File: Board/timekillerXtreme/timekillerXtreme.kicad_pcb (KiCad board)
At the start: 2 copper layers, 61.5 x 105.2 mm, 98 parts, among them J1 Battery, J10 Conn_01x02, J11 TP_USB, J12 PROG, J13 CONN_01X03, J14 TP_3.3V, J15 PE7, J16 PE8, J17 PE9, J18 PE10, J19 PD4, J2 USB_OTG, J20 PD1, J21 PD0, J22 PD3, J23 PE11, J24 Pb12, J3 Conn_Bottom_Expansion, J4 Conn_Internal_Expansion, J5 Conn_LCD_Board, J6 uSD, J7 CAPTEST, J8 TP_AUDIO_R, J9 TP_AUDIO_L, Q1 IRLML6302, Q2 PMBT3904.215, SW1 PWR, SW2 A, SW3 B, SW4 LEFT, SW5 RIGHT, SW6 DOWN, SW7 UP, SW8 RST, U1 MCP73831, U2 FT230XS-R, U3 NCP1529, U5 STM32F407VGT6, U6 USBLC6, U7 AOZ1310, U8 USBLC6, U9 USBLC6, Y1 32.768 KHz, Y2 16MHz

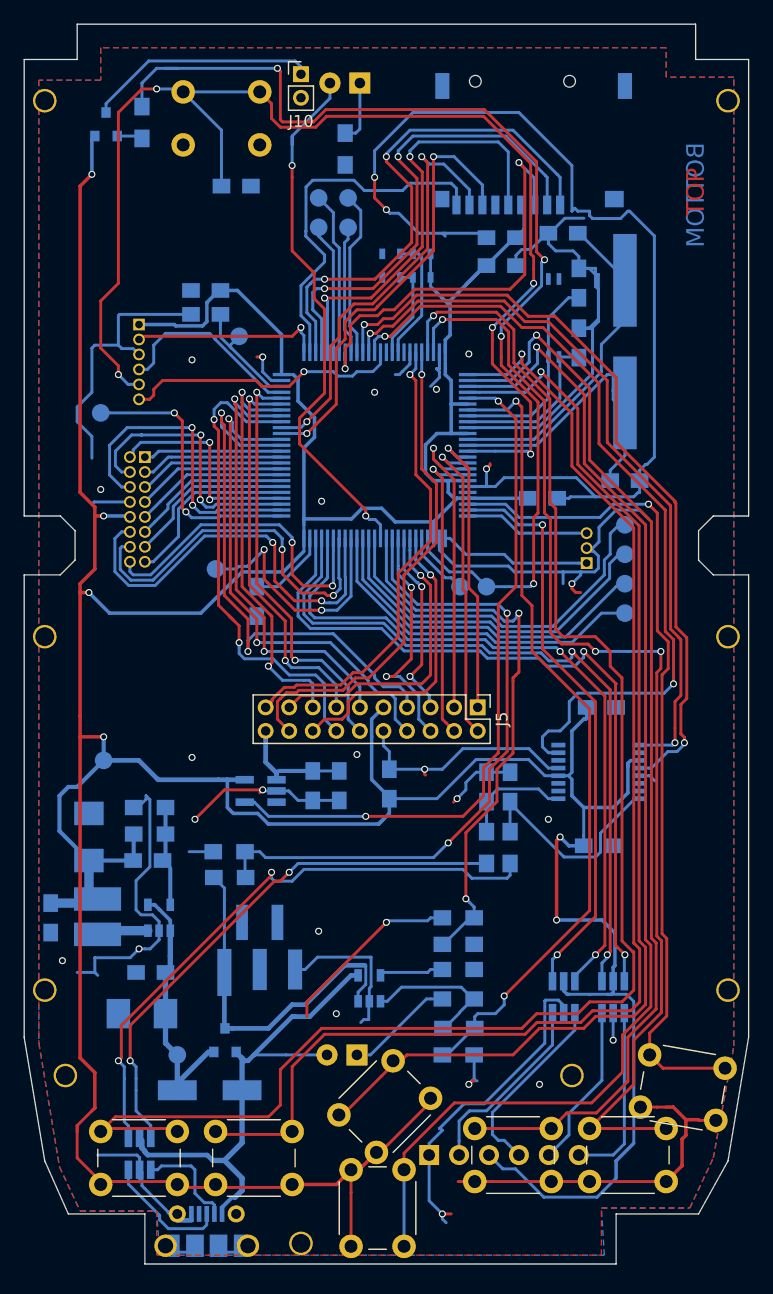
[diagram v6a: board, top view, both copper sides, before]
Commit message: First round of modifications for rev.1
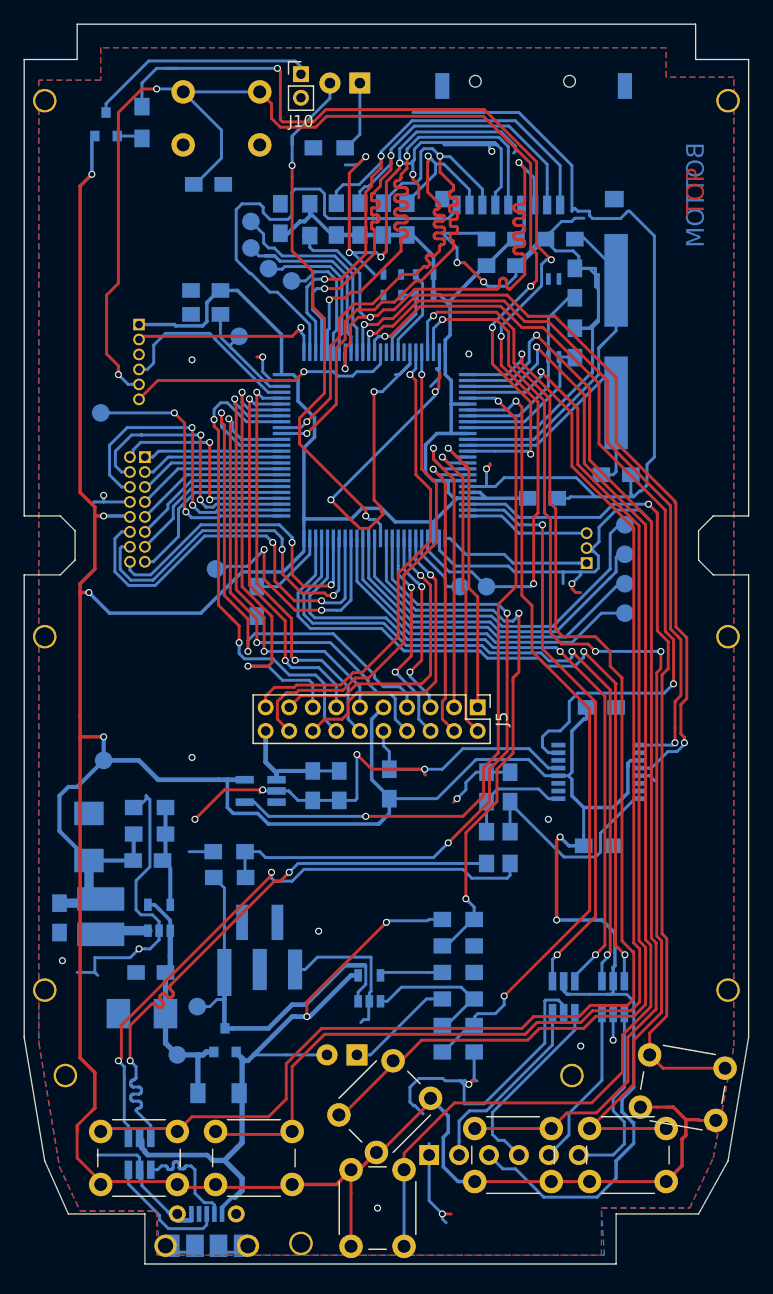
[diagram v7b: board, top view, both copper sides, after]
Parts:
- added C7: 100n, Capacitors_SMD:C_0805_HandSoldering, B.Cu at (139.2, 56.5)
- added J25: TP_BATT, Measurement_Points:Measurement_Point_Round-SMD-Pad_Small, B.Cu at (132.2, 123.4)
- added R20: 47k, Resistors_SMD:R_0805_HandSoldering, B.Cu at (146.0, 56.5)
- added R21: 47k, Resistors_SMD:R_0805_HandSoldering, B.Cu at (141.8, 56.6)
- added R22: 47k, Resistors_SMD:R_0805_HandSoldering, B.Cu at (148.0, 56.5)
- added R23: 47k, Resistors_SMD:R_0805_HandSoldering, B.Cu at (150.0, 56.5)
- added R7: 47k, Resistors_SMD:R_0805_HandSoldering, B.Cu at (144.0, 56.5)
- C10, C9: value 4p -> 3.3p
- C11, C12: value 8p -> 8.2p
- C33: value 22u -> 2.2u
- D2: footprint Diodes_SMD:D_MiniMELF_Handsoldering -> Diodes_SMD:D_MiniMELF
- R19: value 2k -> 0
- moved J19 8.49 mm to (136.8, 56.8)
- moved J22 8.43 mm to (136.8, 59.0)
- moved J20 7.35 mm to (138.2, 60.8)
- moved J21 5.10 mm to (140.2, 61.8)
- moved C13 2.35 mm to (133.2, 53.6)
- moved R10 1.77 mm to (151.5, 61.2)
- moved R11 1.75 mm to (148.8, 61.2)
- moved R17 1.52 mm to (151.5, 63.0)
- moved R18 1.50 mm to (148.8, 63.0)
- moved R16 1.35 mm to (143.4, 50.5), turned to 180 degrees
- moved C12 0.90 mm to (167.8, 78.2)
- moved D2 0.79 mm to (134.0, 130.8)
- moved C4 0.75 mm to (120.5, 115.9)
- moved Y2 0.75 mm to (167.8, 67.0)
- moved C11 0.56 mm to (163.0, 58.2)
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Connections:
- C29 pad 1: Net-(C29-Pad1) -> GND
- C29 pad 2: GND -> Net-(C29-Pad2)
- J7 pad 1: Net-(C29-Pad1) -> Net-(C29-Pad2)
- U5 pad 21: Net-(U5-Pad21) -> +3V3
- U5 pad 73: Net-(C29-Pad1) -> Net-(C29-Pad2)
- U9 pad 3: Net-(J3-Pad2) -> Net-(U9-Pad3)
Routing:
- net GND: track 344.2 -> 434.4 mm, vias 25 -> 32
- net +3V3: track 457.1 -> 485.5 mm
- net SD_CMD: track 35.7 -> 53.1 mm, vias 2 -> 3
- net SD_D0: track 38.0 -> 50.9 mm
- net Net-(U9-Pad3): track 0.00 -> 10.6 mm
- net Net-(J3-Pad2): track 16.2 -> 5.57 mm
- net Net-(C29-Pad2): track 0.00 -> 10.2 mm
- net Net-(C29-Pad1): track 10.2 -> 0.00 mm
- net SD_D1: track 36.7 -> 46.9 mm
- net SD_DETECT: track 31.1 -> 39.9 mm
- net SD_D3: track 41.5 -> 47.9 mm
- net Net-(J22-Pad1): track 11.0 -> 17.3 mm
- net BTN_5_A: track 131.3 -> 125.2 mm
- net SD_CK: track 36.9 -> 42.1 mm
- net USB_D-: track 46.2 -> 51.0 mm
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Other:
- board text added: "Beta2 2018-10-14"
- board text added: "Designed by Standa"
- board text added: "SDA-Wonder"
- board text removed: "SDA-Wonder Beta 2018-09-04"

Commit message: Keeping repo up to date.
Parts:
- added F1: 1A, Resistors_SMD:R_0805_HandSoldering, B.Cu at (134.1, 127.0)
- SPKR: renamed from J10; moved to B.Cu
- moved VBATT 11.8 mm to (144.0, 124.2)
- moved SW6 5.06 mm to (144.5, 138.8), turned to 0 degrees
- moved Q1 4.21 mm to (138.8, 126.5)
- moved SW7 2.76 mm to (151.0, 133.8), turned to 180 degrees
- moved D1 2.61 mm to (148.2, 126.8)
- moved C31 2.00 mm to (168.2, 109.8), turned to 180 degrees
- moved C16 1.82 mm to (168.2, 97.5)
- moved PRG 1.21 mm to (127.8, 64.4)
- moved SPKR 1.03 mm to (140.8, 45.2), turned to 180 degrees
- moved U2 0.98 mm to (167.3, 103.5), turned to 90 degrees
- moved V_USB 0.90 mm to (130.0, 128.2)
- moved Y1 0.37 mm to (162.4, 65.0)
- moved D2 0.25 mm to (134.0, 131.0)
- moved J3 0.25 mm to (151.9, 136.2)
- moved SW3 0.25 mm to (172.0, 138.5)
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- renumbered J4 to EXP, J12 to PRG, J14 to V3.3, J25 to VBATT, J7 to VCAP, J11 to V_USB
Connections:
- net Net-(D4-Pad2) renamed SYS_LED
- net Net-(R12-Pad2) renamed VBATT_SENSE
- net Net-(R13-Pad2) renamed VBUS_SENSE
- J1 pad 1: BATT+ -> Net-(F1-Pad2)
- R16 pad 1: Net-(D4-Pad1) -> GND
- R16 pad 2: GND -> Net-(D4-Pad1)
- U9 pad 3: Net-(U9-Pad3) -> Net-(J3-Pad2)
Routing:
- net GND: track 434.4 -> 466.2 mm, vias 32 -> 35
- net USART2_TX: track 66.3 -> 80.1 mm
- net Net-(J3-Pad2): track 5.57 -> 16.3 mm
- net Net-(U9-Pad3): track 10.6 -> 0.00 mm
- net Net-(F1-Pad2): track 0.00 -> 8.52 mm
- net FT23_TXE: track 68.5 -> 60.3 mm
- net +3V3: track 485.5 -> 492.2 mm
- net USART2_RX: track 62.3 -> 67.9 mm
- net BTN_2_DOWN: track 104.8 -> 109.9 mm
- net Net-(C1-Pad2): track 18.6 -> 14.1 mm
- net Net-(C2-Pad2): track 9.51 -> 13.9 mm
- net USB_VBUS: track 62.0 -> 57.9 mm
- net Net-(C3-Pad1): track 20.4 -> 23.9 mm
- net LCD_D6: track 46.4 -> 44.3 mm
- net Net-(D1-Pad1): track 9.22 -> 7.18 mm
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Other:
- board text added: "LCD Connector Board"
